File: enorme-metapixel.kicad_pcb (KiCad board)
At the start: 2 copper layers, 75 x 75 mm, 42 parts, among them J1 VIN, J2 STRIP_0, J3 STRIP_1, J4 STRIP_2, J5 UART, Q1 SSM3K329R, Q2 SSM3K329R, Q3 SSM3K329R, Q4 SSM3K329R, Q5 SSM3K329R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

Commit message: Rev 2
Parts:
- removed kibuzzard-63B86E19: G***, kibuzzard-63B86E19
- removed kibuzzard-63B86EB9 (x3): G***, kibuzzard-63B86EB9
- removed kibuzzard-63B86F04: G***, kibuzzard-63B86F04
- removed kibuzzard-63B89CDD: G***, kibuzzard-63B89CDD
- removed kibuzzard-63B89D08: G***, kibuzzard-63B89D08
- added D2: Ch.0, ENSADLED:ARGB_0404, F.Cu at (176.1, 106.6)
- added D3: Ch.1, ENSADLED:ARGB_0404, F.Cu at (159.1, 106.6)
- added D4: Ch.2, ENSADLED:ARGB_0404, F.Cu at (159.1, 89.6)
- added H1: M4, MountingHole:MountingHole_4.3mm_M4, F.Cu at (167.6, 98.1)
- added H2: PEG, MountingHole:MountingHole_3.2mm_M3, F.Cu at (167.6, 121.1)
- added R13: 1k, Resistor_SMD:R_0603_1608Metric, F.Cu at (176.4, 113.9)
- added R14: 1k, Resistor_SMD:R_0603_1608Metric, F.Cu at (179.9, 110.4)
- added R15: 1k, Resistor_SMD:R_0603_1608Metric, F.Cu at (183.4, 106.9)
- added R16: 1k, Resistor_SMD:R_0603_1608Metric, F.Cu at (151.8, 106.9)
- added R17: 1k, Resistor_SMD:R_0603_1608Metric, F.Cu at (155.3, 110.4)
- added R18: 1k, Resistor_SMD:R_0603_1608Metric, F.Cu at (158.8, 113.9)
- added R19: 1k, Resistor_SMD:R_0603_1608Metric, F.Cu at (158.8, 82.2)
- added R20: 1k, Resistor_SMD:R_0603_1608Metric, F.Cu at (155.3, 85.8)
- added R21: 1k, Resistor_SMD:R_0603_1608Metric, F.Cu at (151.8, 89.3)
- added R22: 3.3k, Resistor_SMD:R_0603_1608Metric, F.Cu at (174.0, 104.4)
- added R23: 3.3k, Resistor_SMD:R_0603_1608Metric, F.Cu at (175.4, 103.0)
- added R24: 3.3k, Resistor_SMD:R_0603_1608Metric, F.Cu at (172.5, 105.9)
- added R25: 3.3k, Resistor_SMD:R_0603_1608Metric, F.Cu at (161.2, 104.4)
- added R26: 3.3k, Resistor_SMD:R_0603_1608Metric, F.Cu at (162.6, 105.9)
- added R27: 3.3k, Resistor_SMD:R_0603_1608Metric, F.Cu at (159.8, 103.0)
- added R28: 3.3k, Resistor_SMD:R_0603_1608Metric, F.Cu at (161.1, 91.6)
- added R29: 3.3k, Resistor_SMD:R_0603_1608Metric, F.Cu at (159.7, 93.0)
- added R30: 3.3k, Resistor_SMD:R_0603_1608Metric, F.Cu at (162.5, 90.2)
- J1: footprint TerminalBlock:TerminalBlock_bornier-2_P5.08mm -> ENSADLED:fiche_bornier-2_P5.08mm
- J2, J3, J4: footprint TerminalBlock:TerminalBlock_bornier-4_P5.08mm -> ENSADLED:fiche-bornier-4_P5.08mm
- R1, R2, R3, R4, R5, R6, R7, R8, R9: value 10k -> 100k
- moved R10 64.8 mm to (173.3, 76.7), turned to -135 degrees
- moved J1 57.9 mm to (162.6, 70.9)
- moved kibuzzard-63B86E3D 55.2 mm to (162.6, 74.0)
- moved R11 54.7 mm to (189.0, 92.3)
- moved R1 52.2 mm to (177.5, 115.1)
- moved Q1 52.1 mm to (179.7, 117.2)
- moved J4 51.7 mm to (144.8, 75.3)
- moved R2 51.5 mm to (181.0, 111.5)
- moved Q2 51.4 mm to (183.2, 113.7)
- moved G*** 51.4 mm to (139.9, 98.3), turned to -45 degrees
- moved R3 50.8 mm to (184.6, 108.0)
- moved Q3 50.7 mm to (186.7, 110.1)
- moved J2 50.2 mm to (190.3, 120.8)
- moved J5 49.9 mm to (203.6, 94.3)
- moved U2 49.9 mm to (191.1, 74.6)
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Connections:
- Q1 pad 1: /IO15 -> Net-(Q1-G)
- Q2 pad 1: /IO16 -> Net-(Q2-G)
- Q3 pad 1: /IO17 -> Net-(Q3-G)
- Q4 pad 1: /IO18 -> Net-(Q4-G)
- Q5 pad 1: /IO19 -> Net-(Q5-G)
- Q6 pad 1: /IO21 -> Net-(Q6-G)
- Q7 pad 1: /IO22 -> Net-(Q7-G)
- Q8 pad 1: /IO23 -> Net-(Q8-G)
- Q9 pad 1: /IO25 -> Net-(Q9-G)
- R1 pad 1: /IO15 -> Net-(Q1-G)
- R2 pad 1: /IO16 -> Net-(Q2-G)
- R3 pad 1: /IO17 -> Net-(Q3-G)
- R4 pad 1: /IO18 -> Net-(Q4-G)
- R5 pad 1: /IO19 -> Net-(Q5-G)
- R6 pad 1: /IO21 -> Net-(Q6-G)
- R7 pad 1: /IO22 -> Net-(Q7-G)
- R8 pad 1: /IO23 -> Net-(Q8-G)
- R9 pad 1: /IO25 -> Net-(Q9-G)
- U2 pad 10: /IO25 -> unconnected-(U2-IO25-Pad10)
- U2 pad 12: unconnected-(U2-Pad12) -> /ledc6
- U2 pad 13: unconnected-(U2-Pad13) -> /ledc7
- U2 pad 14: unconnected-(U2-Pad14) -> /ledc8
- U2 pad 23: /IO15 -> unconnected-(U2-IO15-Pad23)
- U2 pad 26: unconnected-(U2-Pad26) -> /ledc3
- U2 pad 27: /IO16 -> /ledc4
- U2 pad 28: /IO17 -> /ledc5
- U2 pad 29: unconnected-(U2-Pad29) -> /ledc0
- U2 pad 30: /IO18 -> /ledc1
- U2 pad 31: /IO19 -> /ledc2
- U2 pad 33: /IO21 -> unconnected-(U2-IO21-Pad33)
- U2 pad 36: /IO22 -> unconnected-(U2-IO22-Pad36)
- U2 pad 37: /IO23 -> unconnected-(U2-IO23-Pad37)
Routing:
- net /ledc5: track 0.00 -> 70.5 mm
- net /IO21: track 65.3 -> 0.00 mm, vias 2 -> 0
- net /ledc4: track 0.00 -> 65.3 mm
- net /IO19: track 62.9 -> 0.00 mm, vias 2 -> 0
- net /IO18: track 61.9 -> 0.00 mm, vias 2 -> 0
- net /ledc3: track 0.00 -> 61.0 mm
- net /IO23: track 60.6 -> 0.00 mm, vias 2 -> 0
- net /IO22: track 57.9 -> 0.00 mm, vias 2 -> 0
- net /IO25: track 48.7 -> 0.00 mm, vias 2 -> 0
- net /ledc0: track 0.00 -> 45.5 mm
- net /ledc1: track 0.00 -> 42.7 mm
- net /IO15: track 41.3 -> 0.00 mm
- net /ledc2: track 0.00 -> 38.9 mm
- net /IO16: track 38.0 -> 0.00 mm
- net /IO17: track 35.3 -> 0.00 mm
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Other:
- board text added: "+3V3 TX RX GND"
- board text added: ". G . R . B . V+ ."
- board text added: ". V+ . B . R . G ."
- board text added: "202303"
- board text added: "5V - 24V"
- board text added: "MetaPixel Rev2"
- board text removed: "+3V3 GND TX RX"
- board text removed: "ENSADLED 012023"
- board text removed: "METAPIXEL REV1"

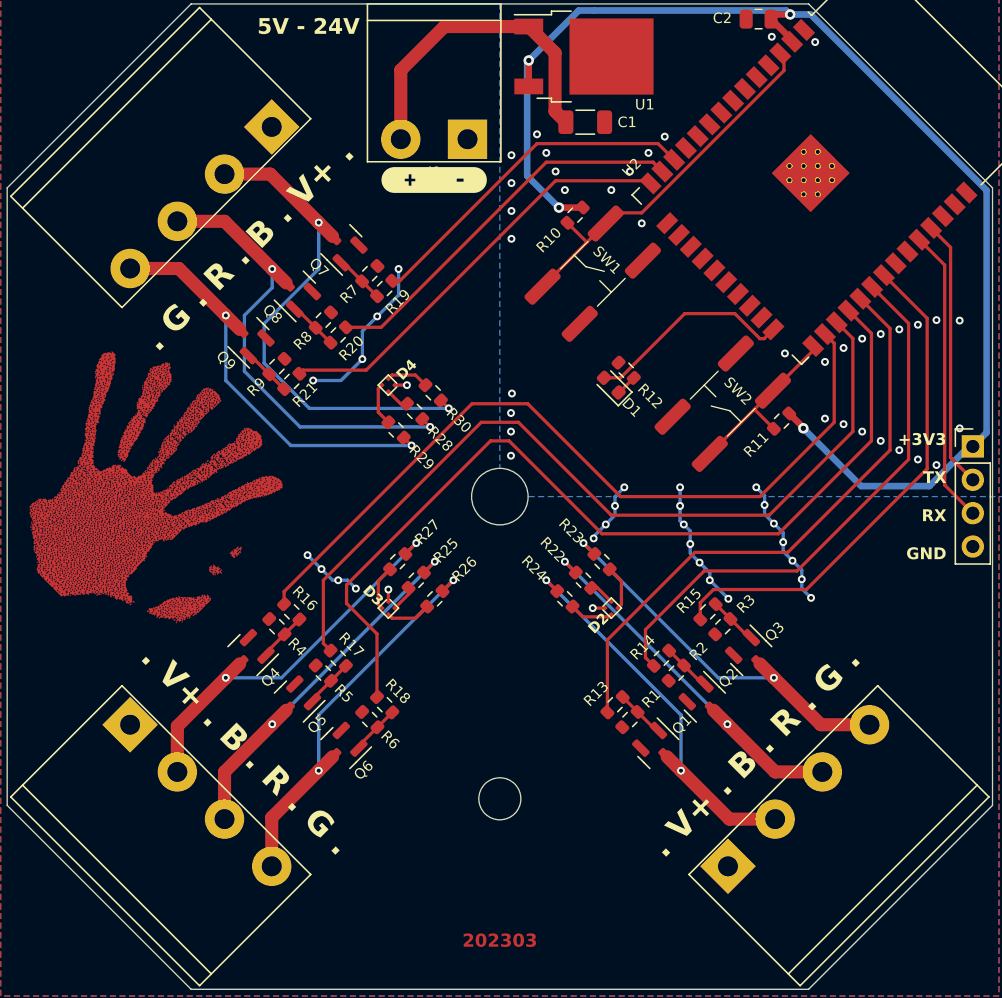
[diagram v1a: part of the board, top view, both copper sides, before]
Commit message: Fix color order
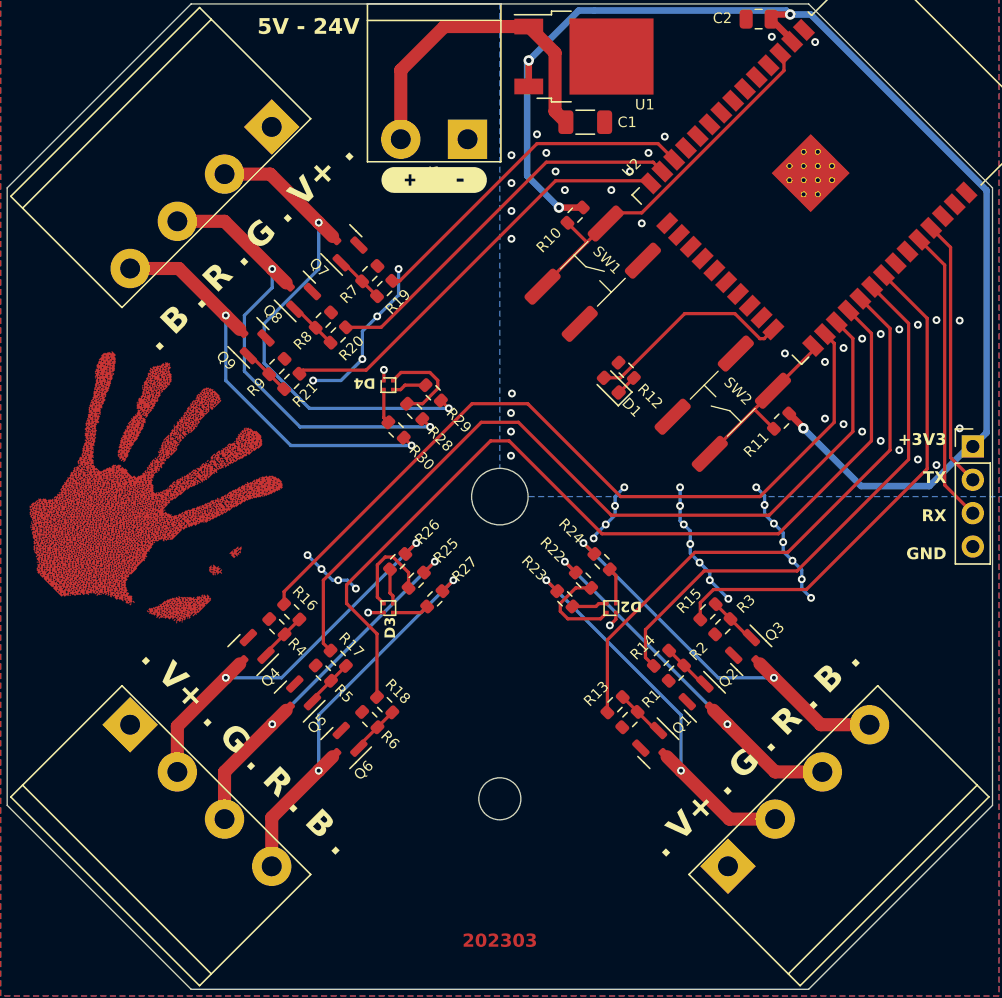
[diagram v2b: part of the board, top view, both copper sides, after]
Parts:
- moved R26 4.00 mm to (159.8, 103.0)
- moved R27 4.00 mm to (162.6, 105.9)
- moved R23 4.00 mm to (172.5, 105.9)
- moved R24 4.00 mm to (175.4, 103.0)
- moved R29 4.00 mm to (162.5, 90.2)
- moved R30 4.00 mm to (159.7, 93.0)
- turned D2 to 90 degrees
- turned D3 to 0 degrees
- turned D4 to -90 degrees
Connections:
- R23 pad 1: /ch0_0 -> /ch0_2
- R24 pad 1: /ch0_2 -> /ch0_0
- R26 pad 1: /ch1_0 -> /ch1_2
- R27 pad 1: /ch1_2 -> /ch1_0
- R29 pad 1: /ch2_0 -> /ch2_2
- R30 pad 1: /ch2_2 -> /ch2_0
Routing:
- net Net-(D4-RK): track 1.80 -> 7.37 mm
- net Net-(D3-RK): track 1.97 -> 7.43 mm
- net Net-(D2-RK): track 1.97 -> 7.41 mm
- net Net-(D3-GK): track 3.44 -> 2.70 mm
- net Net-(D2-GK): track 3.44 -> 2.70 mm
- net Net-(D4-GK): track 3.26 -> 2.63 mm
- net Net-(D4-BK): track 3.26 -> 2.63 mm
- net Net-(D3-BK): track 3.44 -> 2.80 mm
- net Net-(D2-BK): track 3.35 -> 2.80 mm
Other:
- board text added: ". B . R . G . V+ ."
- board text added: ". V+ . G . R . B ."
- board text removed: ". G . R . B . V+ ."
- board text removed: ". V+ . B . R . G ."

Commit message: Rev 3
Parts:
- removed D2: Ch.0, ENSADLED:ARGB_0404
- removed D3: Ch.1, ENSADLED:ARGB_0404
- removed D4: Ch.2, ENSADLED:ARGB_0404
- removed R22, R23, R24, R25, R26, R27, R28, R29, R30: 3.3k, Resistor_SMD:R_0603_1608Metric
- added ?: , clipboard:b081e147-b981-4ee1-b835-e472bfd32432, B.Cu at (139.8, 98.1)
- added C3: 10µF 30V, Capacitor_SMD:C_0603_1608Metric, F.Cu at (159.8, 78.4)
- added C4: 10µF 5V, Capacitor_SMD:C_0603_1608Metric, F.Cu at (174.1, 73.7)
- added J6: VIN, ENSADLED:fiche_bornier-2_P5.08mm, F.Cu at (163.1, 66.6)
- added JP1: 5V_jumper, Jumper:SolderJumper-2_P1.3mm_Open_RoundedPad1.0x1.5mm, F.Cu at (156.7, 70.6)
- added U3: LD1086DT50TR, Package_TO_SOT_SMD:TO-252-2, F.Cu at (165.5, 74.1)
- added kibuzzard-63B86E3D: G***, kibuzzard-63B86E3D, B.Cu at (163.2, 63.1)
- C1: value 1µF -> 1µF 5V; footprint Capacitor_SMD:C_1206_3216Metric -> Capacitor_SMD:C_0603_1608Metric
- J2, J3, J4: footprint ENSADLED:fiche-bornier-4_P5.08mm -> ENSADLED:PLUG_Terminal_01x04_2.54mm
- kibuzzard-63B86E3D: moved to B.Cu
- moved kibuzzard-63B86E3D 15.0 mm to (152.2, 63.1)
- moved J1 11.3 mm to (152.1, 66.6)
- moved R11 10.5 mm to (180.2, 86.7)
- moved R10 10.5 mm to (179.0, 85.5)
- moved J2 4.30 mm to (193.4, 123.9)
- moved J3 4.30 mm to (141.8, 123.9)
- moved J4 4.30 mm to (141.8, 72.3)
- moved C1 3.18 mm to (173.0, 72.6), turned to 45 degrees
- moved SW1 2.05 mm to (176.1, 82.6)
- moved SW2 2.05 mm to (183.1, 89.6)
- moved U1 1.53 mm to (173.9, 66.1), turned to 90 degrees
- moved C2 0.76 mm to (187.6, 62.4), turned to 45 degrees
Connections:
- C1 pad 1: VCC -> +5V
- U1 pad 1: VCC -> +5V
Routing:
- net GND: track 42.2 -> 87.9 mm, vias 62 -> 107
- net /ch2_2: track 38.9 -> 15.0 mm, vias 2 -> 0
- net /ch2_1: track 35.6 -> 14.0 mm, vias 2 -> 0
- net /ch2_0: track 32.3 -> 14.0 mm, vias 2 -> 0
- net +3.3V: track 99.8 -> 81.5 mm
- net /ch0_0: track 31.7 -> 14.0 mm, vias 2 -> 0
- net /ch1_0: track 31.7 -> 14.0 mm, vias 2 -> 0
- net /ch0_2: track 31.6 -> 15.0 mm, vias 2 -> 0
- net /ch1_2: track 31.6 -> 15.0 mm, vias 2 -> 0
- net /ch0_1: track 30.4 -> 14.0 mm, vias 2 -> 0
- net /ch1_1: track 30.4 -> 14.0 mm, vias 2 -> 0
- net +5V: track 0.00 -> 16.2 mm, vias 0 -> 28
- net /ledc5: track 70.5 -> 56.4 mm
- net /ledc4: track 65.3 -> 55.5 mm
- net VCC: track 28.0 -> 19.6 mm, vias 3 -> 0
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- added copper zone on B.Cu, net +5V
- added copper zone on F.Cu, net +5V
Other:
- board text added: "+"
- board text added: "0"
- board text added: "1"
- board text added: "2"
- board text added: "202306"
- board text added: "MetaPixel Rev3"
- board text added: "Mode"
- board text added: "Reset"
- board text added: "V+ G R B"
- board text removed: ". B . R . G . V+ ."
- board text removed: ". V+ . G . R . B ."
- board text removed: "202303"
- board text removed: "MetaPixel Rev2"

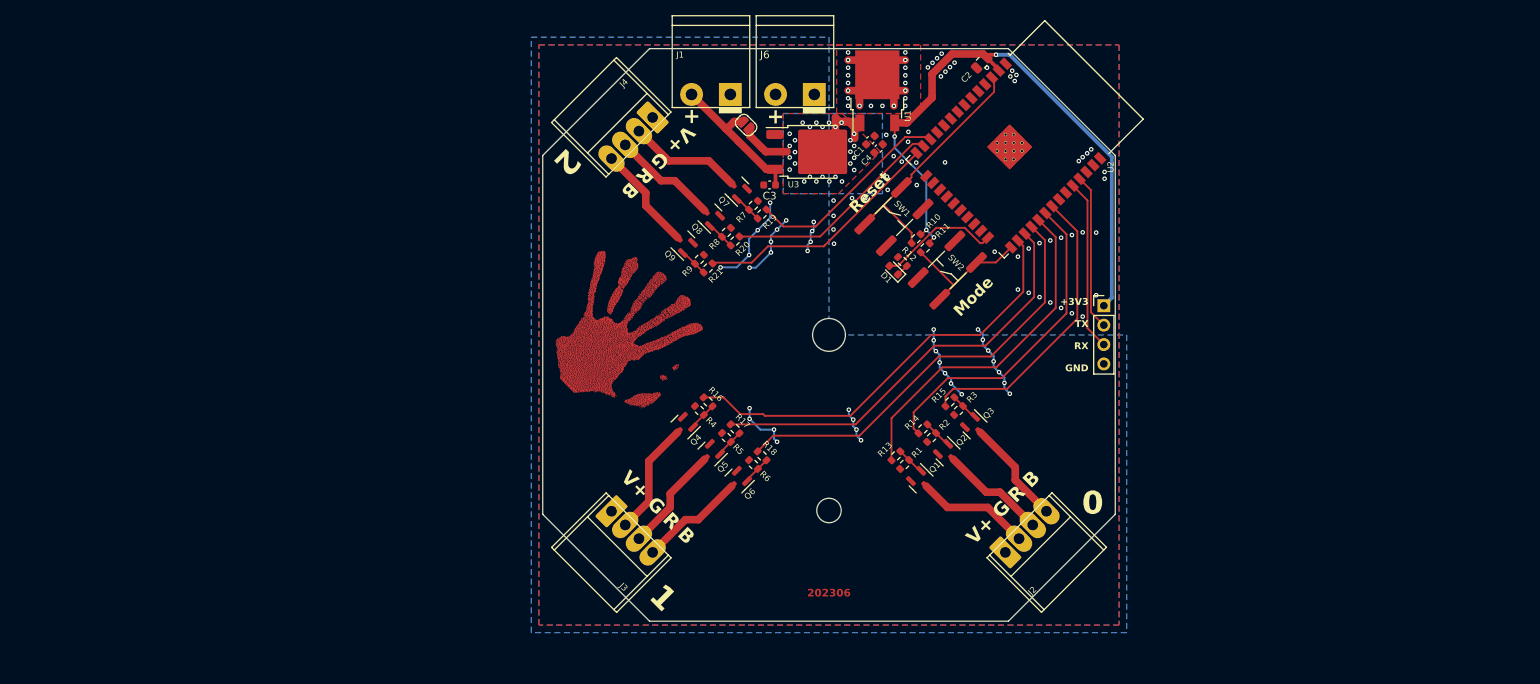
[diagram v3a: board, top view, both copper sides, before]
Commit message: Rev 4 (replace LDO with buck converter)
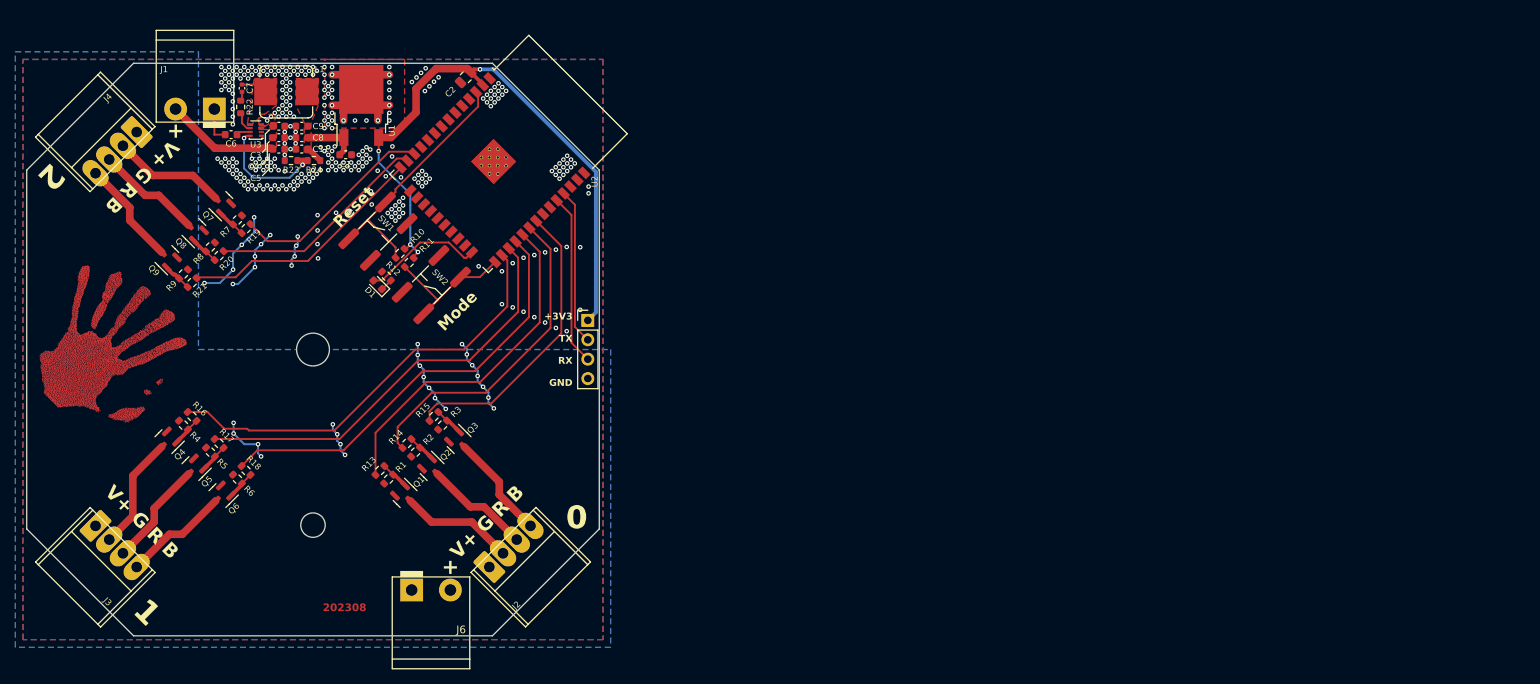
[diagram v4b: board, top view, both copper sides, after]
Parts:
- removed ?: , clipboard:b081e147-b981-4ee1-b835-e472bfd32432
- removed JP1: 5V_jumper, Jumper:SolderJumper-2_P1.3mm_Open_RoundedPad1.0x1.5mm
- added C11: 100nF 50V X7R, Capacitor_SMD:C_0603_1608Metric, F.Cu at (98.5, 73.7)
- added C5: 100nF 50V X7R, Capacitor_SMD:C_0603_1608Metric, F.Cu at (95.5, 73.8)
- added C6: 33nF 50V X7R, Capacitor_SMD:C_0603_1608Metric, F.Cu at (89.3, 71.8)
- added C7: 0.1µF 25V X5R, Capacitor_SMD:C_0402_1005Metric, F.Cu at (90.7, 65.8)
- added C8: 22µF 10V X5R, Capacitor_SMD:C_0603_1608Metric, F.Cu at (98.5, 72.2)
- added C9: 22µF 10V X5R, Capacitor_SMD:C_0603_1608Metric, F.Cu at (98.5, 70.7)
- added L1: 6.8µH, Inductor_SMD:L_Bourns_SRP7028A_7.3x6.6mm, F.Cu at (96.5, 66.2)
- added R22: 5R 5%, Resistor_SMD:R_0603_1608Metric, F.Cu at (90.5, 68.2)
- added R23: 10K 1%, Resistor_SMD:R_0603_1608Metric, F.Cu at (97.1, 75.2)
- added R24: 52.3K 1%, Resistor_SMD:R_0603_1608Metric, F.Cu at (100.1, 75.2)
- C3: value 10µF 30V -> 10µF 35V X5R
- C4: value 10µF 5V -> 10µF 35V X5R
- D1: value LED -> USER LED BLUE
- U3: value LD1086DT50TR -> TPS62933DRLR; footprint Package_TO_SOT_SMD:TO-252-2 -> Package_TO_SOT_SMD:SOT-583-8
- moved J6 80.5 mm to (115.5, 131.5), turned to 0 degrees
- moved C4 78.6 mm to (95.5, 72.2), turned to 0 degrees
- moved U3 73.1 mm to (92.5, 71.2), turned to 180 degrees
- moved C1 68.8 mm to (104.3, 74.5), turned to 0 degrees
- moved C2 67.6 mm to (120.0, 64.3)
- moved D1 67.6 mm to (108.5, 91.5)
- moved J1 67.6 mm to (84.5, 68.5)
- moved J2 67.6 mm to (125.8, 125.8)
- moved J3 67.6 mm to (74.2, 125.8)
- moved J4 67.6 mm to (74.2, 74.2)
- moved Q2 67.6 mm to (115.6, 115.6)
- moved Q5 67.6 mm to (84.4, 115.6)
- moved Q8 67.6 mm to (84.4, 84.4)
- moved R12 67.6 mm to (109.6, 90.4)
- moved R14 67.6 mm to (112.3, 112.3)
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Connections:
- C4 pad 1: +5V -> VCC
- U3 pad 1: GND -> unconnected-(U3-RT-Pad1)
- U3 pad 2: +5V -> unconnected-(U3-EN-Pad2)
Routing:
- net /FB: track 0.00 -> 16.2 mm, vias 0 -> 2
- net +5V: track 16.2 -> 9.52 mm, vias 28 -> 0
- net GND: track 87.9 -> 92.9 mm, vias 107 -> 332
- net VCC: track 19.6 -> 14.7 mm
- net /SW: track 0.00 -> 4.22 mm
- net /BST: track 0.00 -> 2.63 mm
- net /SS: track 0.00 -> 2.06 mm
- net /BST_C: track 0.00 -> 1.15 mm
- added copper zone on F.Cu, net /SW
- added copper zone on F.Cu, net VCC
- removed copper zone on B.Cu, net +5V
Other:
- board text added: "202308"
- board text added: "MetaPixel Rev4"
- board text removed: "202306"
- board text removed: "MetaPixel Rev3"
